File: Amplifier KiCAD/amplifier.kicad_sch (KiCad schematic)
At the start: 7 parts, among them J1 Conn_01x03_Pin, J10 PA_IN, J11 EQ_OUT, J12 Speakers, J2 Main Power In, J8 Power To Amp, J9 Power In

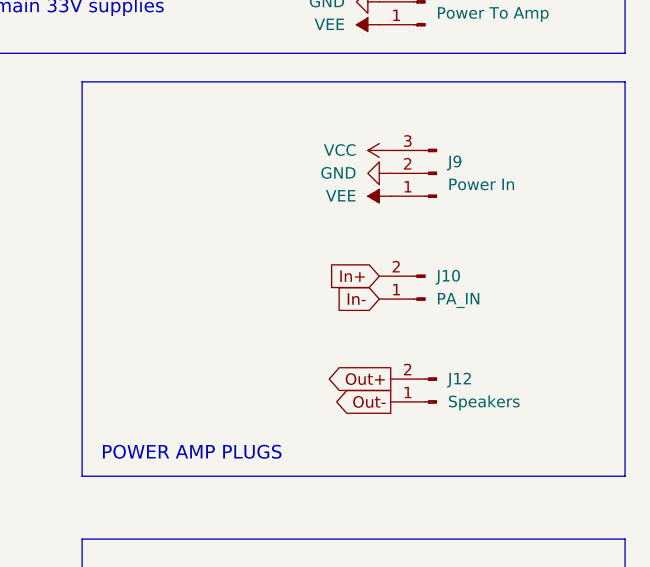
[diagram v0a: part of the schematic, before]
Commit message: Component Placement Finalised, Starting Traces
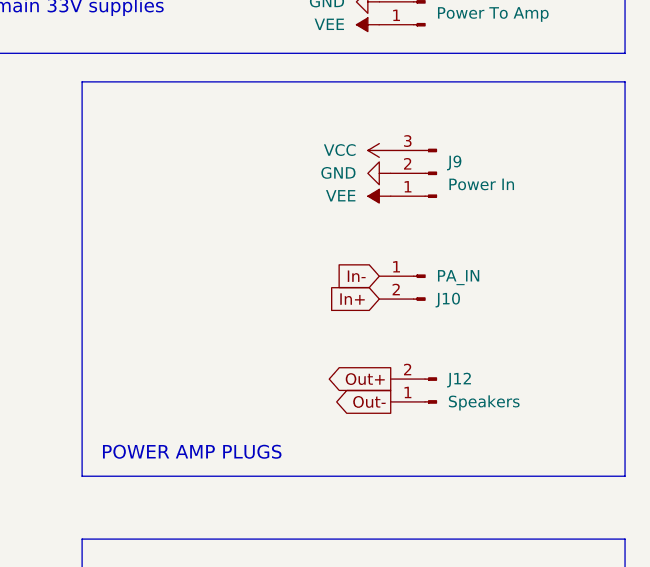
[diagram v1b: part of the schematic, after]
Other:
- moved on the sheet: J10
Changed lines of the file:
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@@
 	(global_label "In+"
 		(shape input)
-		(at 254 87.63 180)
-		(fields_autoplaced yes)
-		(effects
-			(font
-				(size 1.27 1.27)
-			)
-			(justify right)
-		)
-		(property "Intersheetrefs" "${INTERSHEET_REFS}"
-			(at 247.6886 87.63 0)
+		(at 254 90.17 180)
+		(fields_autoplaced yes)
+		(effects
+			(font
+				(size 1.27 1.27)
+			)
+			(justify right)
+		)
+		(property "Intersheetrefs" "${INTERSHEET_REFS}"
+			(at 247.6886 90.17 0)
 			(hide yes)
 			(show_name no)
@@
 	(global_label "In-"
 		(shape input)
-		(at 254 90.17 180)
-		(fields_autoplaced yes)
-		(effects
-			(font
-				(size 1.27 1.27)
-			)
-			(justify right)
-		)
-		(property "Intersheetrefs" "${INTERSHEET_REFS}"
-			(at 247.6886 90.17 0)
+		(at 254 87.63 180)
+		(fields_autoplaced yes)
+		(effects
+			(font
+				(size 1.27 1.27)
+			)
+			(justify right)
+		)
+		(property "Intersheetrefs" "${INTERSHEET_REFS}"
+			(at 247.6886 87.63 0)
 			(hide yes)
 			(show_name no)
@@
 	(symbol
 		(lib_id "Connector:Conn_01x02_Pin")
-		(at 259.08 90.17 180)
+		(at 259.08 87.63 0)
+		(mirror y)
 		(unit 1)
 		(body_style 1)
@@
 		(in_pos_files yes)
 		(dnp no)
-		(fields_autoplaced yes)
 		(property "Reference" "J10"
-			(at 260.35 87.6299 0)
+			(at 260.35 90.1701 0)
 			(show_name no)
 			(do_not_autoplace no)
@@
 		)
 		(property "Value" "PA_IN"
-			(at 260.35 90.1699 0)
+			(at 260.35 87.6301 0)
 			(show_name no)
 			(do_not_autoplace no)
@@
 		)
 		(property "Footprint" "Connector_JST:JST_PH_B3B-PH-K_1x03_P2.00mm_Vertical"
-			(at 259.08 90.17 0)
+			(at 259.08 87.63 0)
 			(hide yes)
 			(show_name no)
@@
 		)
 		(property "Datasheet" ""
-			(at 259.08 90.17 0)
+			(at 259.08 87.63 0)
 			(hide yes)
 			(show_name no)
@@
 		)
 		(property "Description" "Generic connector, single row, 01x02, script generated"
-			(at 259.08 90.17 0)
-			(hide yes)
-			(show_name no)
+			(at 259.08 87.63 0)
+			(hide yes)
+			(show_name no)

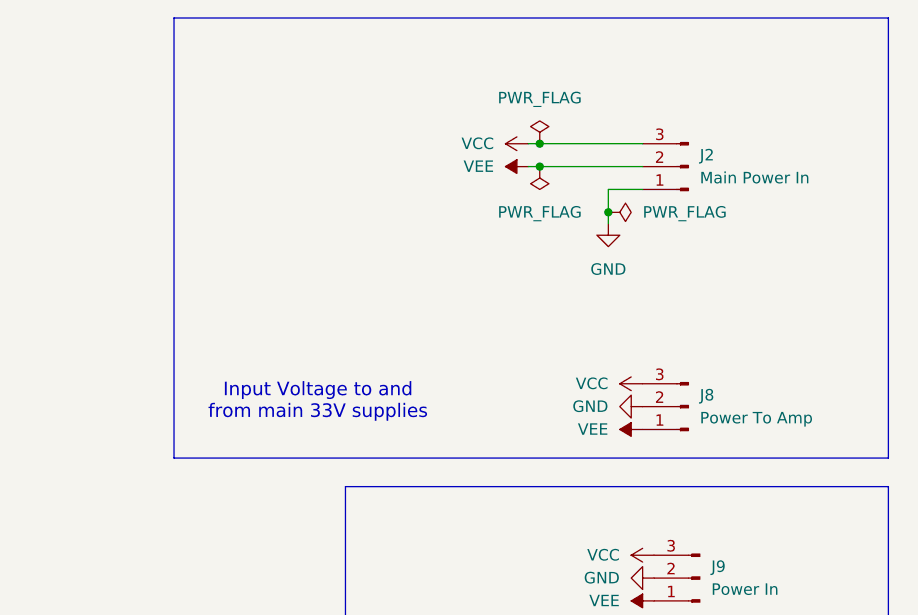
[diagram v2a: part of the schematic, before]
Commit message: Added decoupling capacitors, finished traces, moved I2C jack closer to microcontroller. TODO: Check footprints a final time, check trace thickness, check capacitor locations
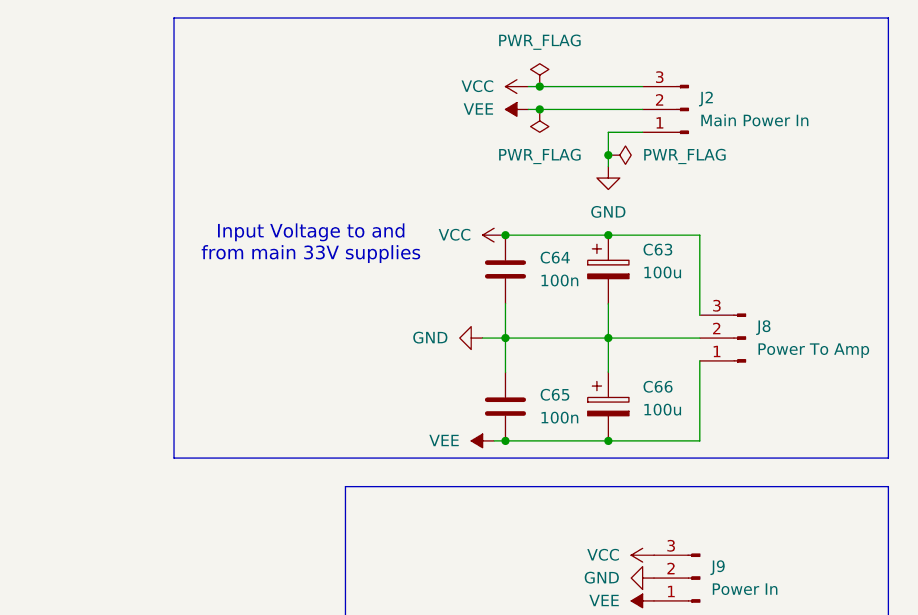
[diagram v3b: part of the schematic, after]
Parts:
- added C63, C66: 100u, Capacitor_THT:CP_Radial_D6.3mm_P2.50mm, symbol Device:C_Polarized
- added C64, C65: 100n, Capacitor_THT:C_Rect_L7.2mm_W2.5mm_P5.00mm, symbol Device:C
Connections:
- net GND: now also C63.2, C64.1, C65.2, C66.1
- net VCC: now also C63.1, C64.2
- net VEE: now also C65.1, C66.2
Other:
- moved on the sheet: J2, J8
